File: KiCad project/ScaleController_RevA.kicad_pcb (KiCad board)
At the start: 4 copper layers, 89.9 x 52.8 mm, 55 parts, among them J1 USB_C_Receptacle, J3 MTMM-103-03-T-S-150, J5 MTMM-103-03-T-S-150, J6 Conn_01x05, J7 MTMM-103-03-T-S-150, J8 MTMM-103-03-T-S-150, J9 Conn_01x04_Socket, Q2 BC817, Q3 BC817, SW1 1101NE, SW2 1101NE, U2 LM1117MPX-3.3_NOPB, U3 ESP32-C3-WROOM-02-H4, U4 CP2102N-A02-GQFN20, U5 USBLC6-2SC6, U6 HX711

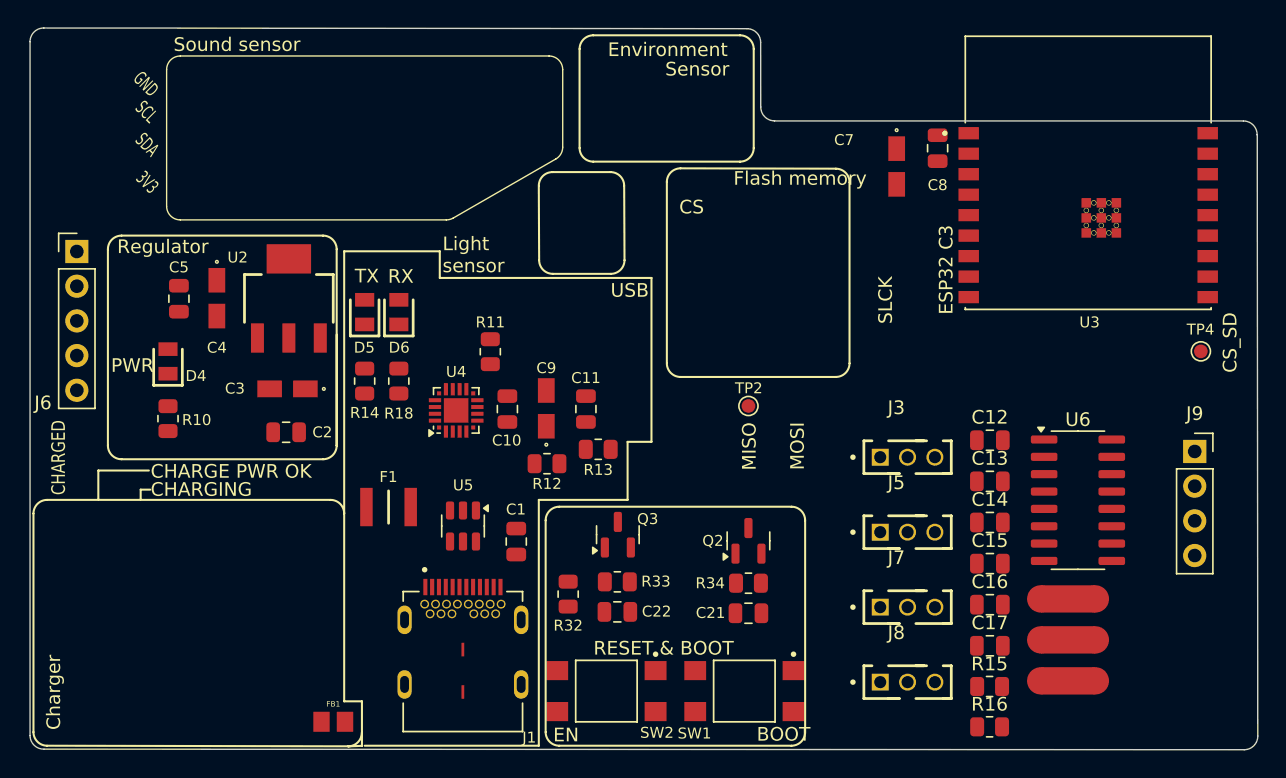
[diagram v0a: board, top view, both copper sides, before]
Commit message: Pre-routing prep: purge legacy silk, add mounting holes, fix net classes
- Removed all 104 board-level F.SilkS graphics/text inherited from the
  KLP-5e board (Charger, Sound sensor, SPI labels, old J6 pinout, ...).
- Added four M3 mounting holes H1-H4 (board-only, excluded from BOM/POS,
  reference text hidden) at (116,76.5) (116.5,119.5) (197,120.5) (169,84).
- Moved FB1 from the bottom edge to beside F1 at (133.3,107) rot 0 so the
  VBUS -> F1 -> FB1 -> U2 chain is straight.
- Net classes: Default and 5V_USB vias 0.3/0.3 -> 0.5/0.3; 5V_USB track
  0.25 -> 0.5 mm; "+5V" assigned to 5V_USB.
- Deleted the In2.Cu VBUS and +5V_USB islands; In2 is now a solid 3.3V
  plane. Those nets route on F.Cu.

DRC: 141 unrouted, 86 violations, all mask/lib-sync/module-outline noise.

Co-Authored-By: Claude Fable 5.1 <noreply@anthropic.com>
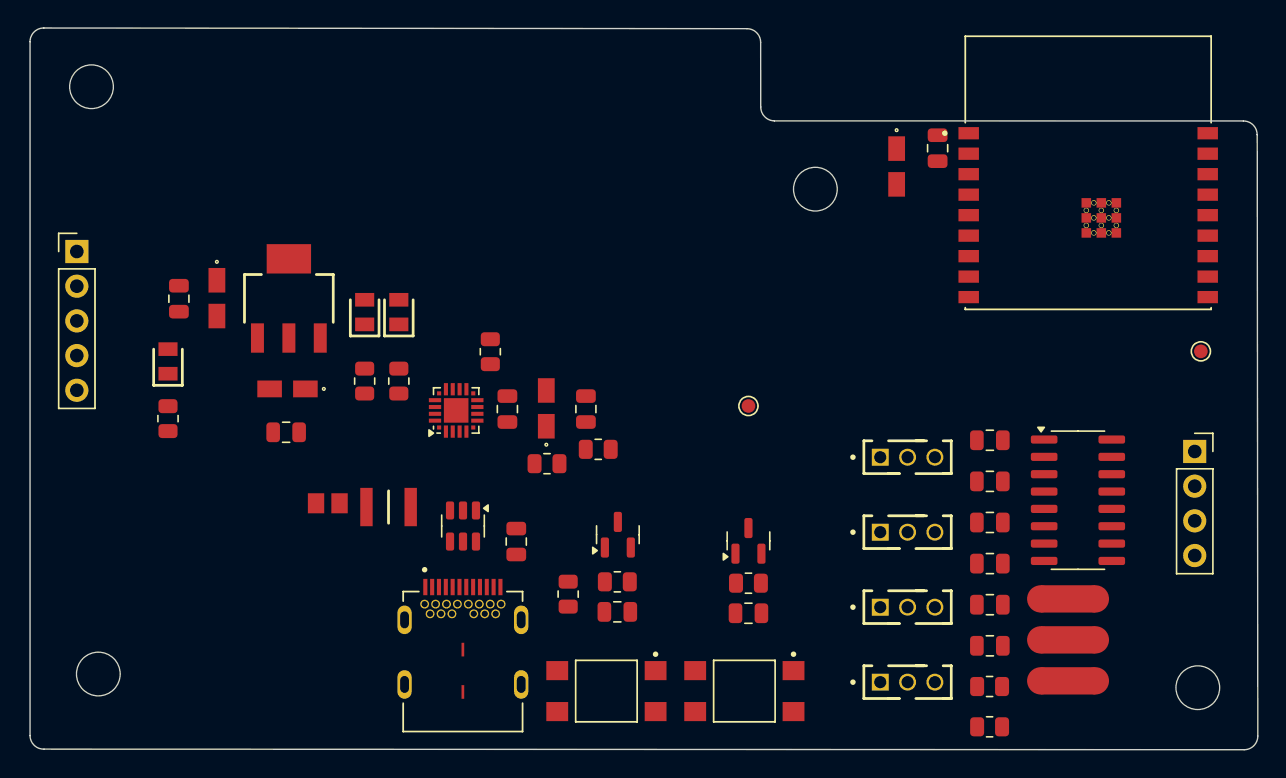
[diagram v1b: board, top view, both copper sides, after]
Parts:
- added H1: MountingHole_3.2mm_M3, MountingHole:MountingHole_3.2mm_M3, F.Cu at (116.0, 76.5)
- added H2: MountingHole_3.2mm_M3, MountingHole:MountingHole_3.2mm_M3, F.Cu at (116.5, 119.5)
- added H3: MountingHole_3.2mm_M3, MountingHole:MountingHole_3.2mm_M3, F.Cu at (197.0, 120.5)
- added H4: b, MountingHole:MountingHole_3.2mm_M3, F.Cu at (169.0, 84.0)
- moved FB1 16.0 mm to (133.3, 107.0), turned to 0 degrees
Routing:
- removed copper zone on In2.Cu, net /+5V_USB
- removed copper zone on In2.Cu, net /VBUS
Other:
- board text removed: "3V3"
- board text removed: "BOOT"
- board text removed: "CHARGE PWR OK"
- board text removed: "CHARGED"
- board text removed: "CHARGING"
- board text removed: "CS"
- board text removed: "CS_SD"
- board text removed: "Charger"
- board text removed: "EN"
- board text removed: "ESP32 C3"
- board text removed: "Environment"
- board text removed: "Flash memory"
- board text removed: "GND"
- board text removed: "Light sensor"
- board text removed: "MISO"
- board text removed: "MOSI"
- board text removed: "PWR"
- board text removed: "RESET & BOOT"
- board text removed: "RX"
- board text removed: "Regulator"
- board text removed: "SCL"
- board text removed: "SDA"
- board text removed: "SLCK"
- board text removed: "Sensor"
- board text removed: "Sound sensor"
- board text removed: "TX"
- board text removed: "USB"

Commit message: Route power chain: VBUS, +5V_USB, +5V, local 3.3V; two 3.3V vias to In2
First routing chunk, all F.Cu: J1 VBUS pads (0.3 mm stubs) -> U5 -> F1
and C1 -> R12; F1 -> FB1; FB1 -> C2 -> C3 -> U2 in; U2 out -> tab ->
C4 -> C5 -> D4, with two 0.6/0.4 vias from the tab onto the In2.Cu 3.3V
plane. J6 pin 1 now reaches 3.3V through the plane.

DRC: 126 unrouted (was 141), 86 violations, all cosmetic. One +5V
track has a small gap to close.

Co-Authored-By: Claude Fable 5.1 <noreply@anthropic.com>
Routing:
- net /VBUS: track 0.00 -> 27.5 mm
- net 3.3V: track 0.00 -> 24.7 mm, vias 0 -> 2
- net +5V: track 0.00 -> 9.89 mm
- net /+5V_USB: track 0.00 -> 2.08 mm

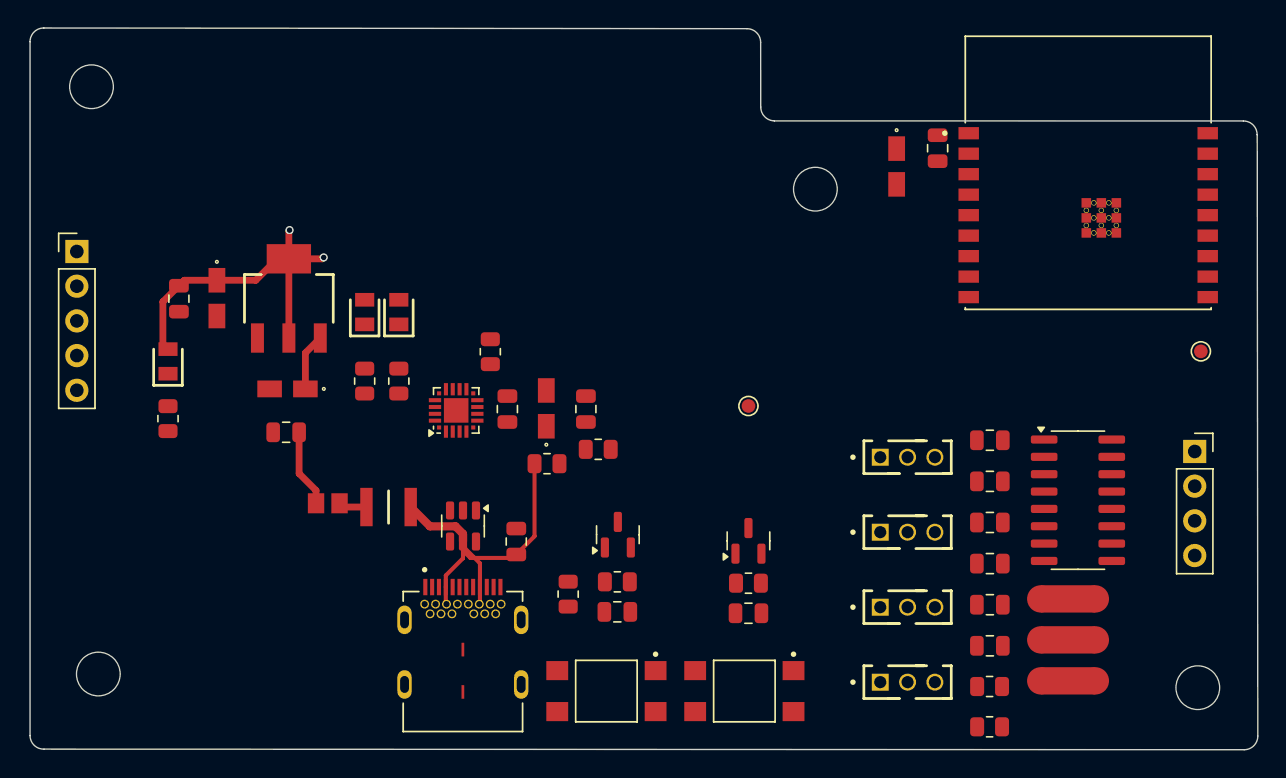
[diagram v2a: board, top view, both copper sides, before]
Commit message: Route 3.3V distribution: F.Cu links per cluster, vias to In2 plane
Closed the +5V gap (C2 -> C3). Routed 3.3V clusters on F.Cu with a via
to the In2.Cu plane at each: CP2102N (U4 pads 6/7 -> C10 -> C9, R11,
R32, D5/D6), ESP32-C3 (U3 pin 1 -> C8 -> C7), HX711 (U6 pins 1/3/16,
C14-C16, NT2). J1 footprint now allows bridged solder-mask apertures
(0.5 mm pitch), clearing 53 mask-bridge errors.

DRC: 107 unrouted (was 126). Two vias at (192.5,102.5) and (184.5,118)
are 0.4/0.2 and must be resized to 0.6/0.4.

Co-Authored-By: Claude Fable 5.1 <noreply@anthropic.com>
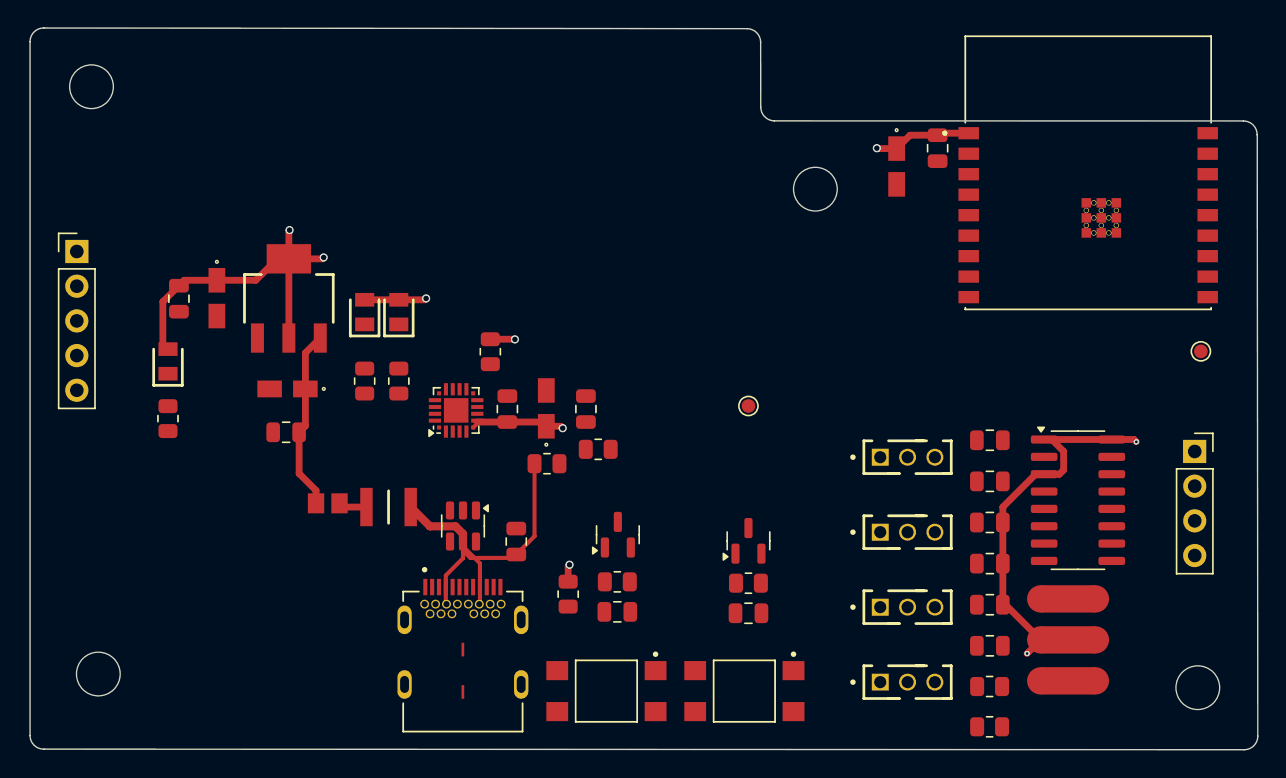
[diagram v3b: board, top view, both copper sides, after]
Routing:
- net 3.3V: track 24.7 -> 74.5 mm, vias 2 -> 9
- net +5V: track 9.89 -> 13.3 mm

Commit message: Route GND: via to In1 plane at every SMD ground pad
41 GND connections closed: stub-and-via at each SMD GND pad (25 vias,
0.6/0.4), J1 A1/A12 tied to the PTH shell pins below them, G3/G4 tied to
the S1-S4 shell legs, U4 GND pins into its exposed pad, ESP32-C3 module
ground grid linked by short tracks. Resized the two 0.4/0.2 3.3V vias
to 0.6/0.4.

DRC: 66 unrouted (was 107), 34 violations, all lib-sync/module-outline.

Co-Authored-By: Claude Fable 5.1 <noreply@anthropic.com>
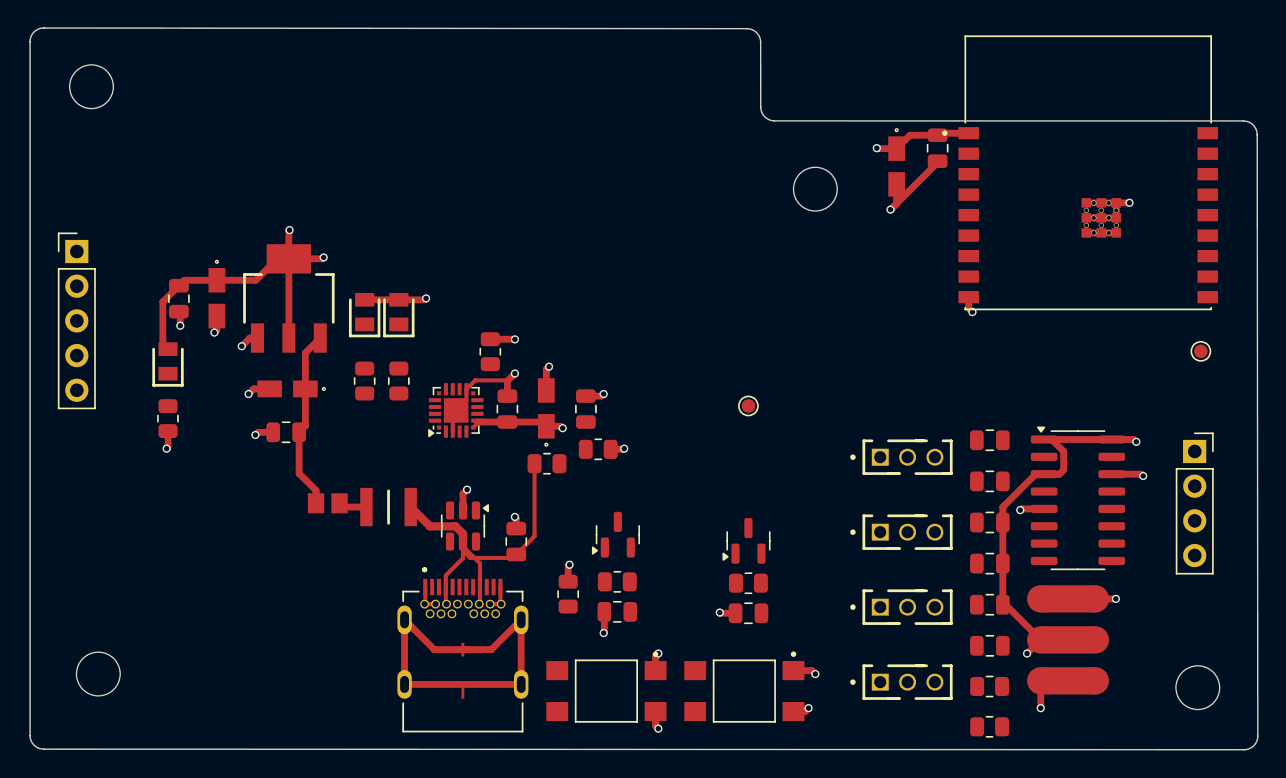
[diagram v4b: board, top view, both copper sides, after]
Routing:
- net GND: track 0.00 -> 90.6 mm, vias 0 -> 25

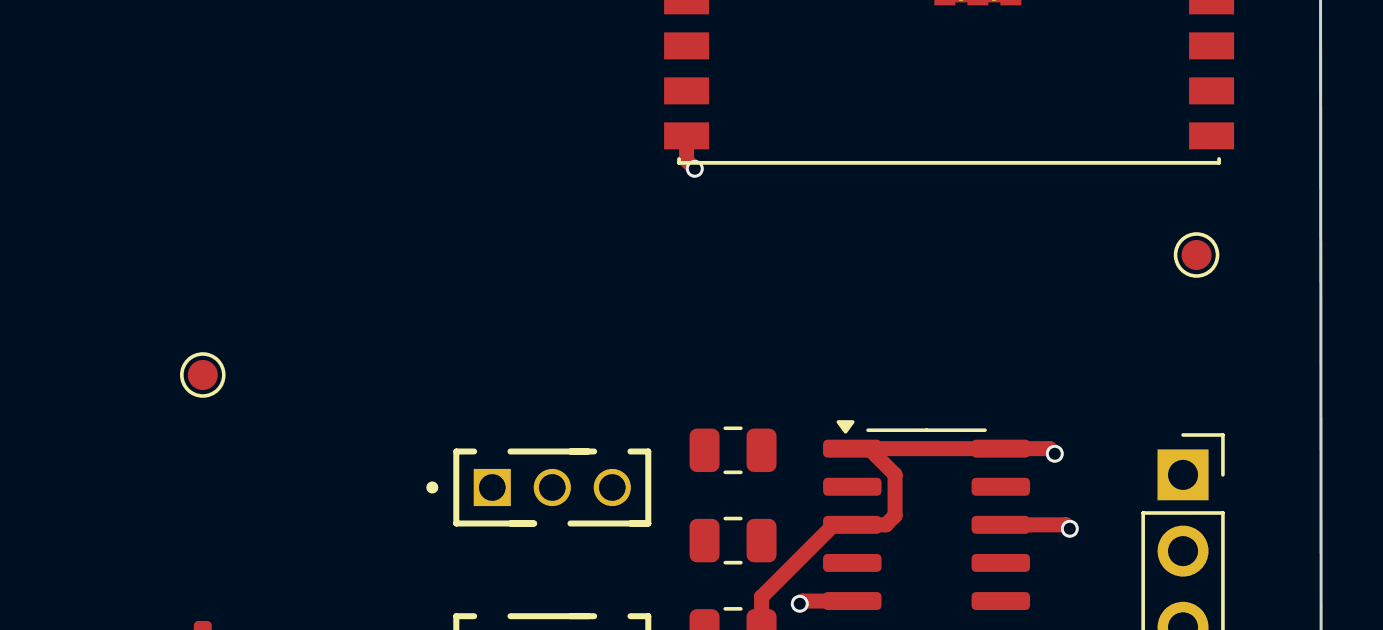
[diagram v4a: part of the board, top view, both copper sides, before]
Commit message: Fix HX711 input filter topology; remove stale test points
C12/C13 were in series with the load-cell signal (S -> 100R -> 4.7nF ->
INA), which blocks the DC bridge output. R15/R16 now feed INA+/INA-
directly and C12/C13 shunt those nodes to AGND. Removed TP2 (DOUT) and
TP4 (PD_SCK), leftovers from the KLP-5e board. Netlist: 64 nets, ERC 0
errors. PCB updated from schematic; 66 unrouted, DRC unchanged.

Co-Authored-By: Claude Fable 5.1 <noreply@anthropic.com>
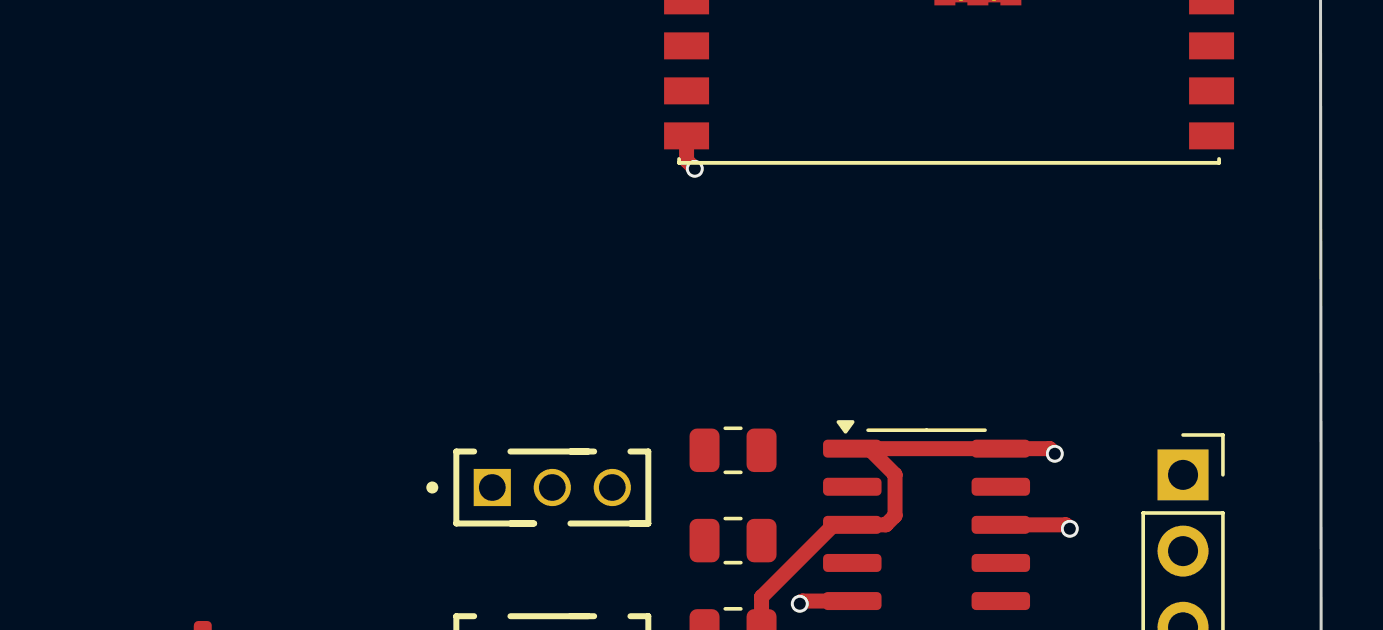
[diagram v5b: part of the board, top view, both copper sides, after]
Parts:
- removed TP2: Test MISO, TestPoint:TestPoint_Pad_D1.0mm
- removed TP4: TEST CS_SD, TestPoint:TestPoint_Pad_D1.0mm
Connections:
- C12 pad 1: Net-(C12-Pad1) -> /HX711_LoadCell_Summing/AGND
- C13 pad 2: Net-(C13-Pad2) -> /HX711_LoadCell_Summing/AGND
- R15 pad 1: Net-(C12-Pad1) -> /HX711_LoadCell_Summing/A+
- R16 pad 1: Net-(C13-Pad2) -> /HX711_LoadCell_Summing/A-
